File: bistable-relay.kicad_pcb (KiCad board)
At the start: 2 copper layers, 21.2 x 11.1 mm, 9 parts, among them J1 edge_connector, K1 FH44L-1AT-L1-DC5V, U1 MIC4427

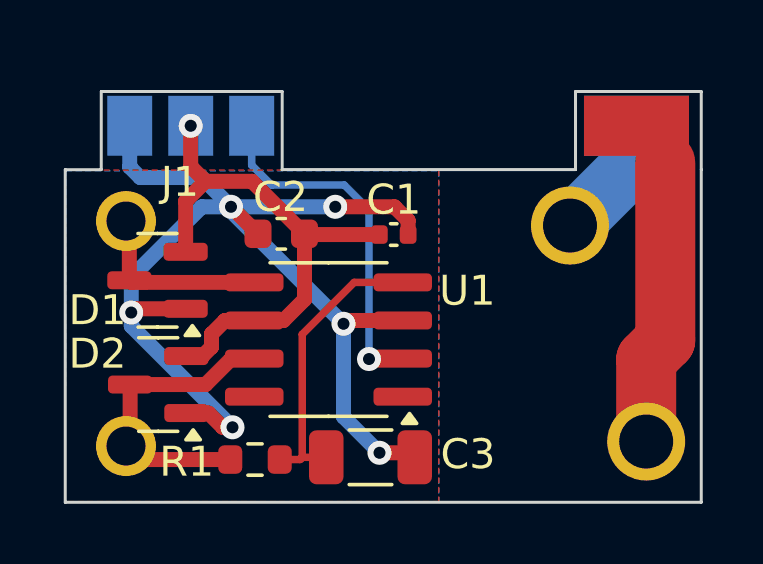
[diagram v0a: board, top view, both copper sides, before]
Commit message: make board safer by using proper clearence distances
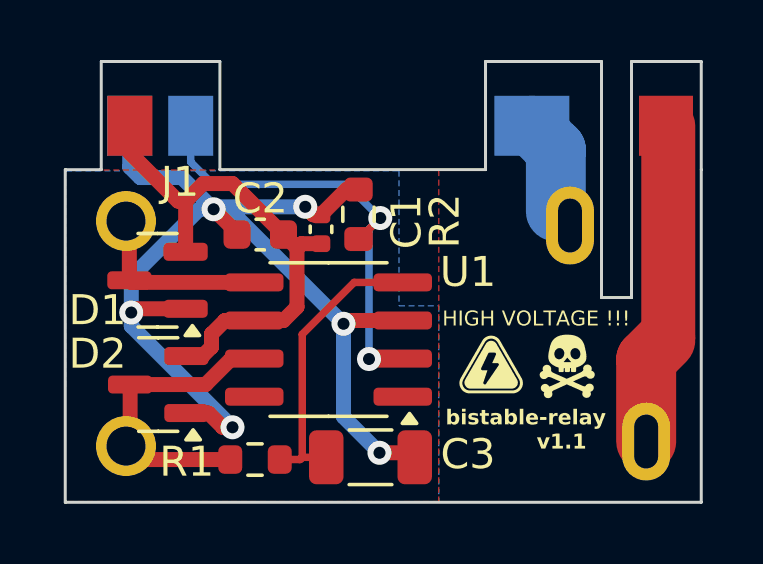
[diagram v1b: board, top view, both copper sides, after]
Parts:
- added R2: 10k, Resistor_SMD:R_0603_1608Metric, F.Cu at (139.7, 96.5)
- moved C1 2.43 mm to (138.4, 97.0), turned to 90 degrees
- moved C2 0.70 mm to (136.4, 97.1)
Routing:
- net Net-(J1-REL): track 11.7 -> 15.3 mm, vias 1 -> 2
- net GND: track 40.7 -> 38.6 mm
- net VCC: track 18.4 -> 17.4 mm, vias 1 -> 0
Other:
- outline, holes or cut-outs redrawn
- board text added: "FABRICATION NOTES 1. PCB THICKNESS 1 mm"
- board text added: "HIGH VOLTAGE !!!"
- board text added: "bistable-relay v1.1"
